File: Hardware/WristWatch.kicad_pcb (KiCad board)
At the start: 2 copper layers, 32 x 32 mm, 100 parts, among them J1 vcc, J2 gnd, J3 vcc, J4 gnd, Q1 Q_PMOS_GSD, U3 LIS2DE12, U4 AP2205-3.0, U5 MCP73832-2-OT, U6 ESP32-C3, Y2 40M, Y3 32.768k

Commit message: Rev C hardware, gerbers, etc. Possible hardware bug flashing or with WiFi.
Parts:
- removed C14: 4u7, Capacitor_SMD:C_0402_1005Metric
- removed C16: 12p, Capacitor_SMD:C_0402_1005Metric
- removed C20, C22: 100n, Capacitor_SMD:C_0402_1005Metric
- removed the C21 at (-2.03, 3.30)
- removed the C21 at (2.03, 3.30)
- removed J3: vcc, TestPoint:TestPoint_Pad_D1.0mm
- removed J4: gnd, TestPoint:TestPoint_Pad_D1.0mm
- removed L2: 3n, Inductor_SMD:L_0402_1005Metric
- removed R12: 100k, Resistor_SMD:R_0402_1005Metric
- added C10: 12p, Capacitor_SMD:C_0402_1005Metric, F.Cu at (0.89, -6.43)
- added C11: 12p, Capacitor_SMD:C_0402_1005Metric, F.Cu at (7.42, 1.82)
- added C2: 2.2u, Capacitor_SMD:C_0402_1005Metric, F.Cu at (-2.51, -3.17)
- added C21: 2.2n, Capacitor_SMD:C_0402_1005Metric, F.Cu at (-3.64, 5.50)
- added C23: 10n, Capacitor_SMD:C_0402_1005Metric, F.Cu at (-5.42, 5.50)
- added C24: 22n, Capacitor_SMD:C_0402_1005Metric, F.Cu at (-7.44, 1.44)
- added C25: 4.7u, Capacitor_SMD:C_0402_1005Metric, F.Cu at (-8.33, 1.44)
- added C26: 22n, Capacitor_SMD:C_0402_1005Metric, F.Cu at (-5.42, 7.28)
- added C27: 470n, Capacitor_SMD:C_0402_1005Metric, F.Cu at (-5.42, 6.39)
- added C3: 100n, Capacitor_SMD:C_0402_1005Metric, F.Cu at (5.79, -2.05)
- added C5: 100n, Capacitor_SMD:C_0402_1005Metric, F.Cu at (-1.32, -0.89)
- added C6: 10u, Capacitor_SMD:C_0402_1005Metric, F.Cu at (-1.32, -1.91)
- added C8: 1.8p, Capacitor_SMD:C_0402_1005Metric, F.Cu at (4.88, -6.43)
- added C9: 12p, Capacitor_SMD:C_0402_1005Metric, F.Cu at (2.77, -6.43)
- added G***: LOGO, LOGO, B.Cu at (5.84, 10.3)
- added L1: 3n, Inductor_SMD:L_0402_1005Metric, F.Cu at (4.37, -5.04)
- added R11: 2.43K, Resistor_SMD:R_0402_1005Metric, F.Cu at (-3.63, -0.97)
- added R13: 100k, Resistor_SMD:R_0402_1005Metric, F.Cu at (-5.33, -5.33)
- added R14: 124k, Resistor_SMD:R_0402_1005Metric, F.Cu at (-3.30, -5.33)
- added R2: 4k7, Resistor_SMD:R_0402_1005Metric, F.Cu at (4.37, 5.00)
- added R3: 4k7, Resistor_SMD:R_0402_1005Metric, F.Cu at (0.81, 5.00)
- added R4: 100k, Resistor_SMD:R_0402_1005Metric, F.Cu at (0.66, 3.22)
- added R5: 100k, Resistor_SMD:R_0402_1005Metric, F.Cu at (0.30, -3.36)
- added TP4: BOOT, TestPoint:TestPoint_Pad_D1.5mm, B.Cu at (11.7, 1.27)
- added TP7: TestPoint, TestPoint:TestPoint_Pad_D1.0mm, B.Cu at (-12.7, 1.14)
- added TP8: TestPoint, TestPoint:TestPoint_Pad_D1.0mm, B.Cu at (-12.7, 3.43)
- added U1: AP2205-3.0, Package_TO_SOT_SMD:SOT-23-5, F.Cu at (-4.29, -3.17)
- C1: value 12p -> 2.2u
- C12: value 1u -> 12p
- C13: value 2u2 -> 470n
- C15: value 4u7 -> 2.2u
- C17: value 10u -> 22n
- C18: value 1.2p -> 220n
- C19: value 1.8p -> 10n
- C4: value 12p -> 100n
- C7: value 12p -> 1.2p
- R1: value 100k -> 10k
- R10: value 10k -> 20K
- R7: value 4k7 -> 3k
- R8: value 4k7 -> 200
- R9: value 10k -> 10K
- TP3: value BOOT -> RST
- TP5: value VCC -> 3v3
- U2: renamed from U6; value ESP32-C3 -> LIS2DE12; footprint Package_DFN_QFN:QFN-32-1EP_5x5mm_P0.5mm_EP3.7x3.7mm -> Package_LGA:LGA-12_2x2mm_P0.5mm
- U3: value LIS2DE12 -> ESP32-C3; footprint Package_LGA:LGA-12_2x2mm_P0.5mm -> Package_DFN_QFN:QFN-32-1EP_5x5mm_P0.5mm_EP3.7x3.7mm
- U4: value AP2205-3.0 -> BQ51050BRHL; footprint Package_TO_SOT_SMD:SOT-23-5 -> Package_DFN_QFN:Texas_VQFN-RHL-20
- U5: value MCP73832-2-OT -> VEML6030; footprint Package_TO_SOT_SMD:SOT-23-5 -> VEML6030:VISHAY_VEML6030_2X2X0.87
- moved TP3 22.7 mm to (11.7, -1.27)
- moved TP1 22.2 mm to (11.7, 3.81)
- moved TP2 22.2 mm to (11.7, 6.35)
- moved TP5 21.9 mm to (11.7, -6.35)
- moved TP6 21.9 mm to (11.7, -3.81)
- moved C12 16.9 mm to (7.42, -1.99), turned to 180 degrees
- moved Q1 14.2 mm to (7.42, 5.00), turned to 0 degrees
- moved U5 13.0 mm to (2.59, 7.45)
- moved C19 12.5 mm to (-1.86, 5.50)
- moved C4 11.4 mm to (4.50, 3.22), turned to 0 degrees
- moved C18 11.3 mm to (-3.64, 6.39)
- moved R6 11.0 mm to (5.77, 5.00), turned to -90 degrees
- moved R7 10.8 mm to (-7.44, -0.46), turned to 90 degrees
- moved R8 8.58 mm to (-8.33, -0.46), turned to 90 degrees
- moved C1 8.14 mm to (-7.09, -2.67)
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- renumbered Y3 to Y1
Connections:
- C1 pad 1: GND -> +BATT
- C1 pad 2: /xtl_ls+ -> GND
- C12 pad 1: +BATT -> GND
- C12 pad 2: GND -> /xtl_hs-
- C13 pad 1: +3V0 -> /BMS/Coil+
- C13 pad 2: GND -> Net-(U4-CLAMP1)
- C15 pad 1: +BATT -> GND
- C15 pad 2: GND -> +BATT
- C17 pad 1: +3V0 -> /BMS/Coil+
- C17 pad 2: GND -> Net-(U4-COMM1)
- C18 pad 1: Net-(U6-LNA_IN) -> Net-(C18-Pad1)
- C18 pad 2: GND -> /BMS/Coil+
- C19 pad 1: Net-(AE1-A) -> /BMS/Coil+
- C19 pad 2: GND -> Net-(U4-BOOT1)
- C4 pad 2: /xtl_ls- -> +3V0
- C7 pad 1: GND -> Net-(U3-LNA_IN)
- C7 pad 2: /xtl_hs+ -> GND
- R1 pad 1: Net-(U6-GPIO8) -> +3V0
- R1 pad 2: +3V0 -> Net-(U2-~{CS})
- R10 pad 1: GND -> /BMS/FOD
- R10 pad 2: Net-(U5-PROG) -> /BMS/RECT
- R7 pad 1: SCL -> /BMS/FOD
- R7 pad 2: +3V0 -> /BMS/ILIM
- R8 pad 1: SDA -> /BMS/FOD
- R8 pad 2: +3V0 -> GND
- R9 pad 1: +3V0 -> Net-(U4-TS/CTRL)
- R9 pad 2: Net-(U3-~{CS}) -> GND
- TP3 pad 1: ESP_BOOT -> /RST
- U2 pad 1: Net-(U6-LNA_IN) -> SCL
- U2 pad 10: unconnected-(U6-MTDI-Pad10) -> +3V0
- U2 pad 11: +3V0 -> unconnected-(U2-INT2-Pad11)
- U2 pad 12: unconnected-(U6-MTCK-Pad12) -> IMU_MOVE_INT
- U2 pad 2: +3V0 -> Net-(U2-~{CS})
- U2 pad 4: /xtl_ls+ -> SDA
- U2 pad 5: /xtl_ls- -> GND
- U2 pad 6: LED_PWR_EN -> GND
- U2 pad 7: Net-(U6-CHIP_EN) -> GND
- U2 pad 8: IMU_MOVE_INT -> GND
- U2 pad 9: IMU_SPAR_INT -> +3V0
- U3 pad 1: SCL -> Net-(U3-LNA_IN)
- U3 pad 10: +3V0 -> ~{BAT_MEAS_EN}
- U3 pad 11: IMU_SPAR_INT -> +3V0
- U3 pad 12: IMU_MOVE_INT -> VEML_SUPPLY
- U3 pad 2: Net-(U3-~{CS}) -> +3V0
- U3 pad 3: unconnected-(U3-SA0/SDO-Pad3) -> +3V0
- U3 pad 4: SDA -> /xtl_ls+
- U3 pad 5: GND -> /xtl_ls-
- U3 pad 6: GND -> LED_PWR_EN
- U3 pad 7: GND -> /RST
- U3 pad 8: GND -> IMU_MOVE_INT
- U3 pad 9: +3V0 -> BAT_MEAS_ADC
- U4 pad 1: +BATT -> GND
- U4 pad 2: GND -> /BMS/Coil+
- U4 pad 3: +BATT -> Net-(U4-BOOT1)
- U4 pad 4: unconnected-(U4-NC-Pad4) -> +BATT
- U4 pad 5: +3V0 -> Net-(U4-CLAMP1)
- U5 pad 1: BMS_STATUS -> GND
- U5 pad 2: GND -> SDA
- U5 pad 3: +BATT -> unconnected-(U5-Pad3)
- U5 pad 4: VBUS -> GND
- U5 pad 5: Net-(U5-PROG) -> SCL
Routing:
- net GND: track 146.1 -> 164.6 mm, vias 22 -> 20
- net +BATT: track 17.1 -> 35.3 mm, vias 1 -> 3
- net /BMS/Coil-: track 0.00 -> 15.2 mm, vias 0 -> 1
- net IMU_SPAR_INT: track 13.9 -> 0.00 mm, vias 2 -> 0
- net /RST: track 0.00 -> 13.6 mm, vias 0 -> 1
- net Net-(C18-Pad1): track 0.00 -> 13.3 mm, vias 0 -> 1
- net VEML_SUPPLY: track 0.00 -> 12.0 mm, vias 0 -> 2
- net VBUS: track 8.86 -> 0.00 mm, vias 1 -> 0
- net BAT_MEAS_ADC: track 0.00 -> 7.68 mm, vias 0 -> 2
- net Net-(U4-COMM2): track 0.00 -> 6.50 mm
- net Net-(U4-COMM1): track 0.00 -> 6.41 mm
- net ~{BAT_MEAS_EN}: track 0.00 -> 5.57 mm, vias 0 -> 2
- net SCL: track 5.15 -> 10.3 mm, vias 0 -> 2
- net /BMS/RECT: track 0.00 -> 5.02 mm, vias 0 -> 2
- net /BMS/Coil+: track 0.00 -> 4.98 mm
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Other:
- board text added: "2.54mm centers"
- board text added: "3v0"
- board text added: "BAT"
- board text added: "BOOT"
- board text added: "C+"
- board text added: "C-"
- board text added: "GND"
- board text added: "RST"
- board text added: "RX"
- board text added: "Rev. C"
- board text added: "TX"
- board text added: "Wristwatch Prototype Rev. C"

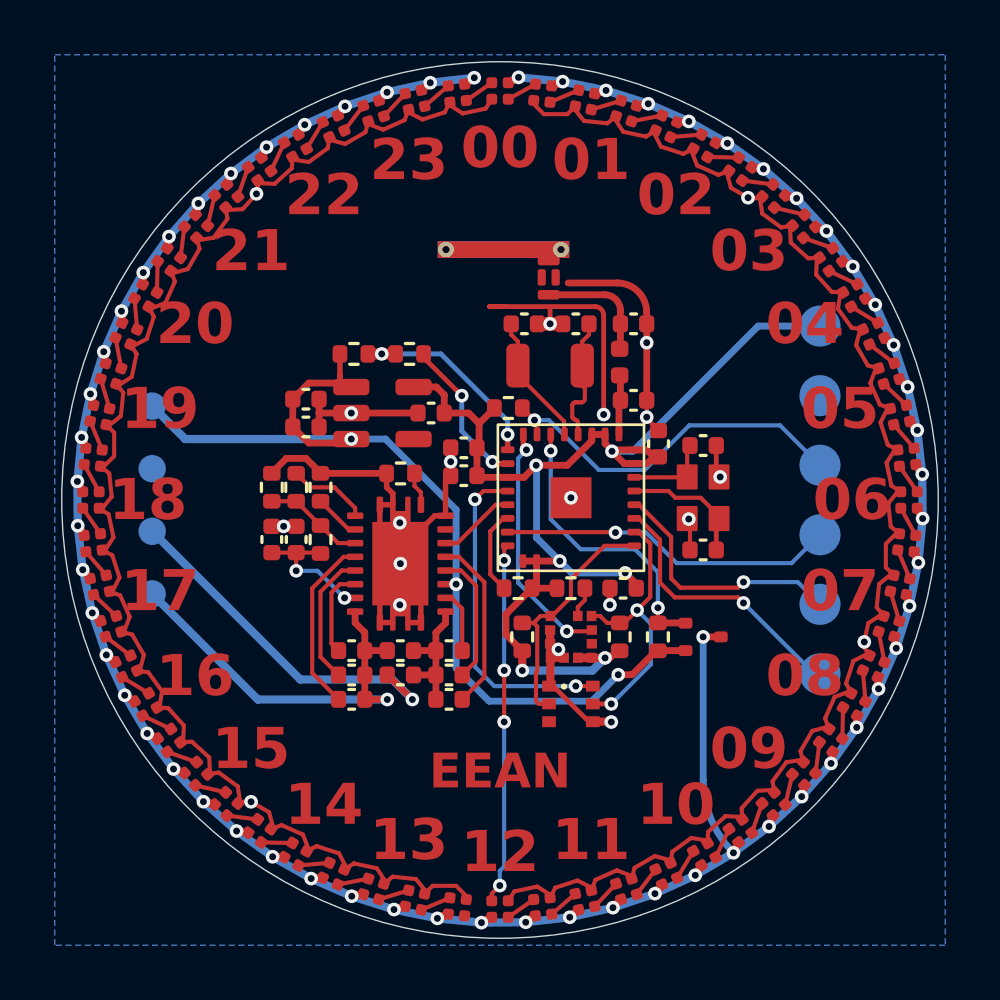
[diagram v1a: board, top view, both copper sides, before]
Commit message: add 100k external pull-up resistor to BMS Status line
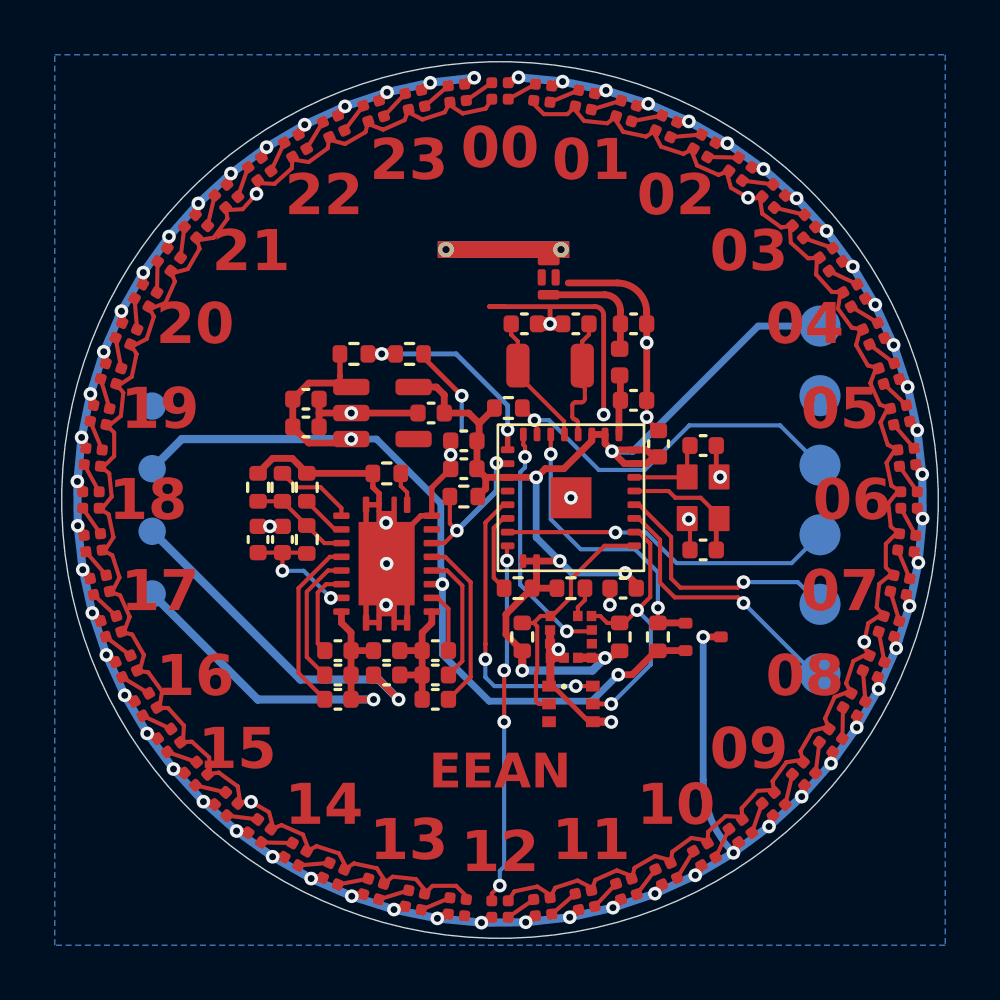
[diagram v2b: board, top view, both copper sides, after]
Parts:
- added R12: 100k, Resistor_SMD:R_0402_1005Metric, F.Cu at (-1.32, -0.13)
- moved J1 2.29 mm to (-12.7, -1.14)
- moved J2 2.29 mm to (-12.7, -3.43)
- moved C24 0.50 mm to (-7.94, 1.44)
- moved R7 0.50 mm to (-7.94, -0.46)
- moved C13 0.50 mm to (-2.36, 6.39)
- moved C17 0.50 mm to (-2.36, 7.28)
- moved C18 0.50 mm to (-4.14, 6.39)
- moved C19 0.50 mm to (-2.36, 5.50)
- moved C21 0.50 mm to (-4.14, 5.50)
- moved R11 0.50 mm to (-4.13, -0.97)
- moved U4 0.50 mm to (-4.14, 2.32)
- moved C23 0.50 mm to (-5.92, 5.50)
- moved C25 0.50 mm to (-8.83, 1.44)
- moved C26 0.50 mm to (-5.92, 7.28)
- moved C27 0.50 mm to (-5.92, 6.39)
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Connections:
- U3 pad 10: ~{BAT_MEAS_EN} -> BMS_STATUS
- U3 pad 12: VEML_SUPPLY -> ~{BAT_MEAS_EN}
- U3 pad 13: BMS_STATUS -> VEML_SUPPLY
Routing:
- net BMS_STATUS: track 2.85 -> 5.94 mm, vias 0 -> 2
- net ~{BAT_MEAS_EN}: track 5.57 -> 3.40 mm, vias 2 -> 1
- net VEML_SUPPLY: track 12.0 -> 10.8 mm
- net /BMS/Coil-: track 15.2 -> 14.7 mm
- net Net-(C18-Pad1): track 13.3 -> 12.8 mm
